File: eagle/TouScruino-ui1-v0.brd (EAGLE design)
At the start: 53.3 x 66 mm, 8 parts, among them U1 TFT_20

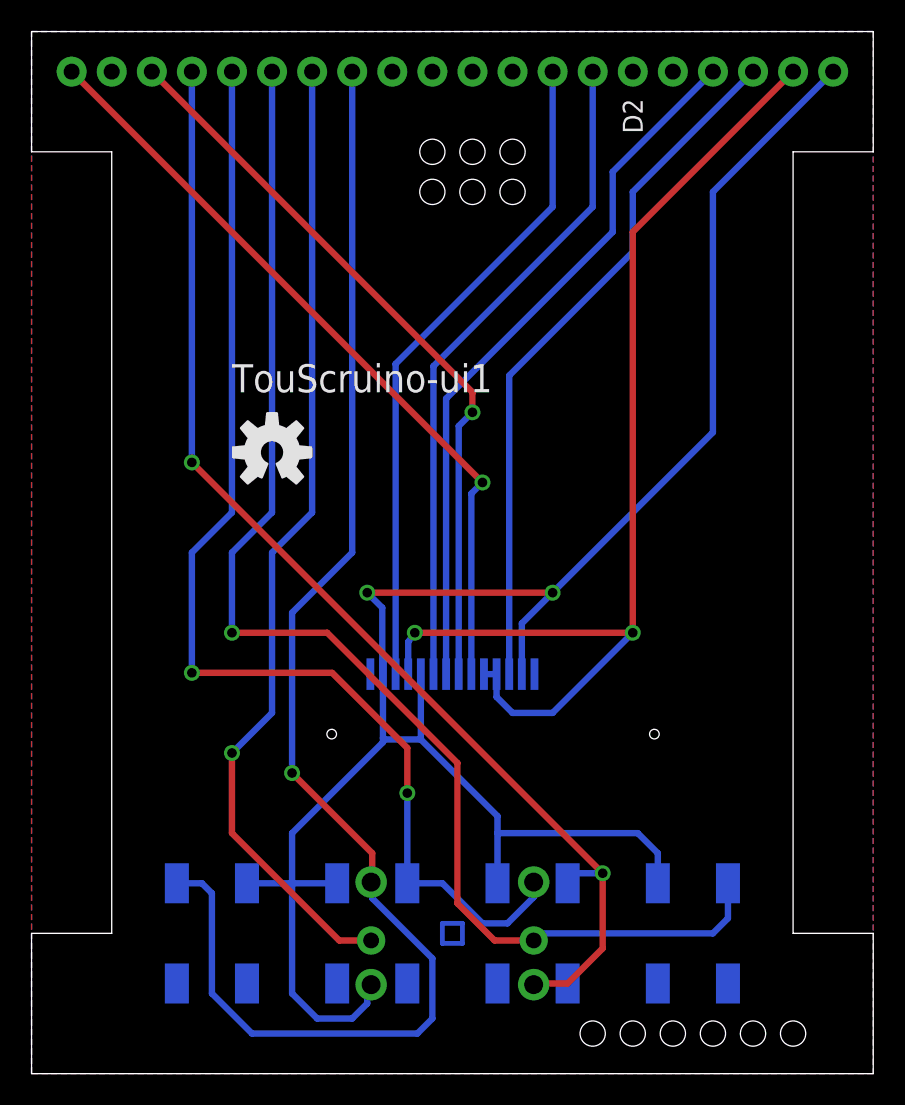
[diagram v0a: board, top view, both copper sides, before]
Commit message: 
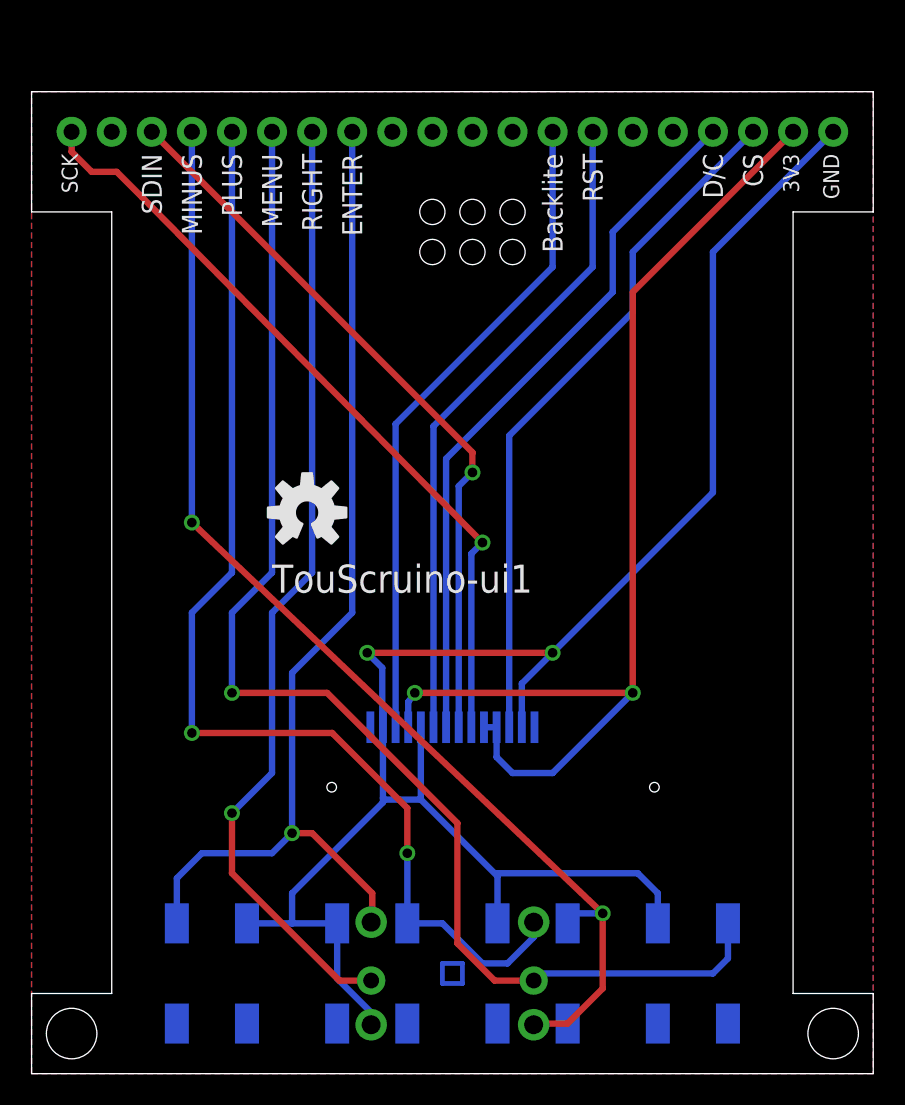
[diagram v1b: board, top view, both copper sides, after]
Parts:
- moved U$3 4.41 mm to (17.5, 35.6)
- moved U1 3.81 mm to (2.54, 59.7)
- moved LCD1 3.37 mm to (26.7, 35.1)
- moved S.ENTER 2.54 mm to (11.4, 6.35)
- moved S.MENU 2.54 mm to (41.9, 6.35)
- moved S.MINUS 2.54 mm to (31.8, 6.35)
- moved S.PLUS 2.54 mm to (21.6, 6.35)
- moved U$4 2.54 mm to (26.7, 6.35)
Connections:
- net D11/MOSI renamed DATA
- net D13/SCK renamed SCK
- net D21 renamed CS
- net D31 renamed D/C
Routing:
- net D14/ENTER: track 89.7 -> 66.0 mm
- net GND: track 129.4 -> 121.1 mm
- net D16/MENU: track 84.1 -> 82.9 mm
- net D15/RIGHT: track 62.0 -> 60.7 mm
- net D17/PLUS: track 74.1 -> 72.8 mm
- net D18/MINUS: track 74.3 -> 73.4 mm
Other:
- board size 53.3 x 66 mm -> 53.3 x 62.2 mm
- board text added: "3V3"
- board text added: "Backlite"
- board text added: "CS"
- board text added: "D/C"
- board text added: "ENTER"
- board text added: "GND"
- board text added: "MENU"
- board text added: "MINUS"
- board text added: "PLUS"
- board text added: "RIGHT"
- board text added: "RST"
- board text added: "SCK"
- board text added: "SDIN"
- board text removed: "D2"
